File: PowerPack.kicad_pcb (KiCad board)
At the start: 2 copper layers, 79 x 31 mm, 75 parts, among them CN1 XT30PW-M, Q1 WSD3066DN33, U1 IP2368_BZ_VGLIP_C5203723, U2 ME6203A50PG

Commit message: route pcb
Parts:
- C12, C13: value 100nf -> 100nf
- moved U1 0.74 mm to (132.2, 89.2)
- moved R6 0.61 mm to (125.0, 108.1)
- moved CSC1 0.59 mm to (123.7, 89.3)
- moved R2 0.59 mm to (123.7, 90.3)
- moved R8 0.52 mm to (140.5, 108.0)
- moved R23 0.36 mm to (106.8, 106.1)
- moved C11 0.26 mm to (167.9, 106.8)
- moved R25 0.25 mm to (111.8, 106.1)
- moved D1 0.23 mm to (127.3, 95.3)
- moved C3 0.23 mm to (130.9, 95.3)
- moved C13 0.23 mm to (115.5, 101.2)
- moved R22 0.20 mm to (107.5, 101.2)
- moved LED2 0.18 mm to (102.0, 106.8)
- moved R19 0.14 mm to (143.6, 85.9)
- moved R20 0.14 mm to (143.6, 86.9)
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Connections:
- net ISET-MODE renamed Net-(JP1-A)
- JP2 pad 1: BAT-MODE -> Net-(JP2-A)
- R13 pad 1: Net-(U1-BAT_MODE) -> BAT-MODE
- R13 pad 2: BAT-MODE -> Net-(JP2-A)
- U1 pad 46: Net-(U1-BAT_MODE) -> BAT-MODE
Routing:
- net Net-(D3-C): track 0.00 -> 86.8 mm, vias 0 -> 3
- net CIO_CC2: track 0.00 -> 69.4 mm, vias 0 -> 2
- net CIO_CC1: track 0.00 -> 63.5 mm, vias 0 -> 2
- net LED1/SCL: track 0.00 -> 58.5 mm, vias 0 -> 2
- net VBUSR_Source: track 0.00 -> 51.8 mm, vias 1 -> 0
- net LED2/SDA: track 0.00 -> 50.4 mm, vias 0 -> 2
- net Net-(LED1--): track 0.00 -> 50.3 mm, vias 0 -> 2
- net CIO_DN: track 0.00 -> 49.7 mm
- net CIO_DP: track 0.00 -> 47.4 mm, vias 0 -> 2
- net VBUSL_Source: track 0.00 -> 40.0 mm, vias 0 -> 2
- net BAT-MODE: track 0.00 -> 36.9 mm, vias 0 -> 2
- net HLED: track 0.00 -> 31.5 mm, vias 0 -> 2
- net Net-(D3-A): track 0.00 -> 20.3 mm
- net Net-(U1-LG2): track 0.00 -> 20.1 mm
- net Net-(U1-LG1): track 0.00 -> 20.0 mm
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- added copper zone on B.Cu, net GND
- added copper zone on F.Cu, net GND

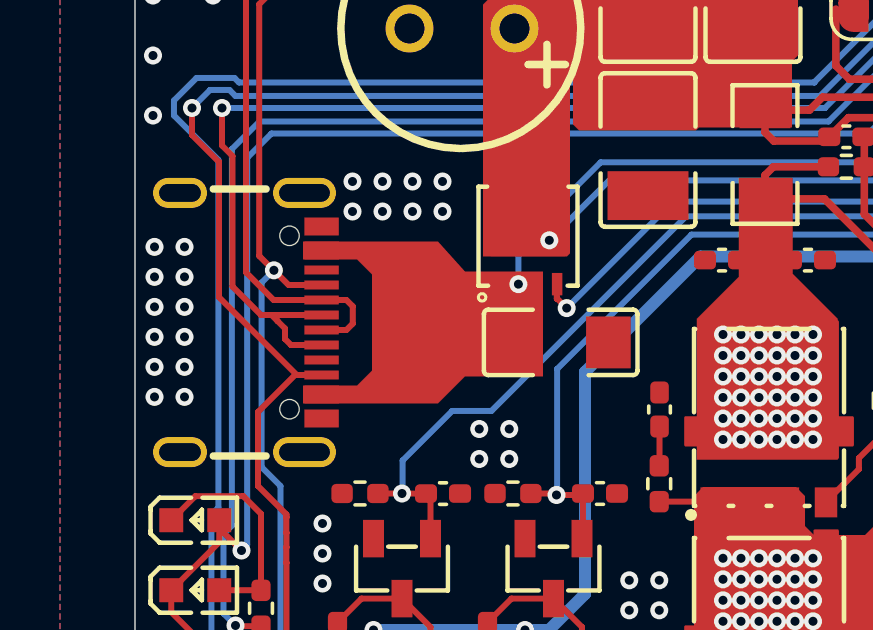
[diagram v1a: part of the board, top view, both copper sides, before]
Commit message: fix usbc connector
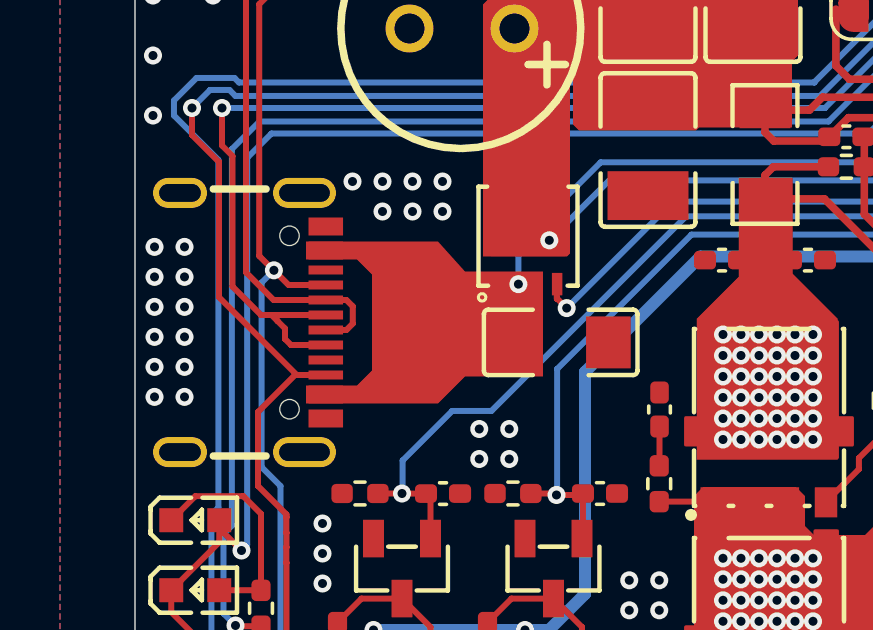
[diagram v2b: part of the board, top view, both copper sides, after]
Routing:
- net GND: vias 240 -> 239
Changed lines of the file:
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@@
 		)
 		(pad "A1B12" smd rect
-			(at -3.2 -2.36 270)
+			(at -3.2 -2.5 270)
 			(size 0.6 1.15)
 			(layers "F.Cu" "F.Mask" "F.Paste")
@@
 		)
 		(pad "A4B9" smd rect
-			(at -2.4 -2.36 270)
+			(at -2.4 -2.5 270)
 			(size 0.6 1.15)
 			(layers "F.Cu" "F.Mask" "F.Paste")
@@
 		)
 		(pad "A5" smd rect
-			(at -1.25 -2.36 270)
+			(at -1.25 -2.5 270)
 			(size 0.3 1.15)
 			(layers "F.Cu" "F.Mask" "F.Paste")
@@
 		)
 		(pad "A6" smd rect
-			(at -0.25 -2.36 270)
+			(at -0.25 -2.5 270)
 			(size 0.3 1.15)
 			(layers "F.Cu" "F.Mask" "F.Paste")
@@
 		)
 		(pad "A7" smd rect
-			(at 0.25 -2.36 270)
+			(at 0.25 -2.5 270)
 			(size 0.3 1.15)
 			(layers "F.Cu" "F.Mask" "F.Paste")
@@
 		)
 		(pad "A8" smd rect
-			(at 1.25 -2.36 270)
+			(at 1.25 -2.5 270)
 			(size 0.3 1.15)
 			(layers "F.Cu" "F.Mask" "F.Paste")
@@
 		)
 		(pad "B1A12" smd rect
-			(at 3.2 -2.36 270)
+			(at 3.2 -2.5 270)
 			(size 0.6 1.15)
 			(layers "F.Cu" "F.Mask" "F.Paste")
@@
 		)
 		(pad "B4A9" smd rect
-			(at 2.4 -2.36 270)
+			(at 2.4 -2.5 270)
 			(size 0.6 1.15)
 			(layers "F.Cu" "F.Mask" "F.Paste")
@@
 		)
 		(pad "B5" smd rect
-			(at 1.75 -2.36 270)
+			(at 1.75 -2.5 270)
 			(size 0.3 1.15)
 			(layers "F.Cu" "F.Mask" "F.Paste")
@@
 		)
 		(pad "B6" smd rect
-			(at 0.75 -2.36 270)
+			(at 0.75 -2.5 270)
 			(size 0.3 1.15)
 			(layers "F.Cu" "F.Mask" "F.Paste")
@@
 		)
 		(pad "B7" smd rect
-			(at -0.75 -2.36 270)
+			(at -0.75 -2.5 270)
 			(size 0.3 1.15)
 			(layers "F.Cu" "F.Mask" "F.Paste")
@@
 		)
 		(pad "B8" smd rect
-			(at -1.75 -2.36 270)
+			(at -1.75 -2.5 270)
 			(size 0.3 1.15)
 			(layers "F.Cu" "F.Mask" "F.Paste")
@@
 	(gr_poly
 		(pts
-			(xy 105.6 92.8) (xy 105.7 92.8) (xy 110.1 92.8) (xy 111 93.8) (xy 113.6 93.8) (xy 113.6 97.3) (xy 111 97.3)
-			(xy 110.1 98.2) (xy 105.6 98.2) (xy 105.6 97.6) (xy 107.4 97.6) (xy 107.9 97.1) (xy 107.9 93.9) (xy 107.4 93.4)
-			(xy 105.6 93.4)
+			(xy 105.7 92.8) (xy 105.7 92.8) (xy 110.1 92.8) (xy 111 93.8) (xy 113.6 93.8) (xy 113.6 97.3) (xy 111 97.3)
+			(xy 110.1 98.2) (xy 105.7 98.2) (xy 105.7 97.6) (xy 107.4 97.6) (xy 107.9 97.1) (xy 107.9 93.9) (xy 107.4 93.4)
+			(xy 105.7 93.4)
 		)
 		(stroke
@@
 	)
 	(segment
-		(start 136.7 90.9)
-		(end 135.62 90.9)
-		(width 0.254)
-		(layer "F.Cu")
-		(net 1)
-	)
-	(segment
 		(start 159.9 102.46)
 		(end 160.9 103.46)
@@
 	)
 	(segment
+		(start 136.7 90.9)
+		(end 135.62 90.9)
+		(width 0.254)
+		(layer "F.Cu")
+		(net 1)
+	)
+	(segment
 		(start 158.4 102.46)
 		(end 159.9 102.46)
@@
 		(size 0.6)
 		(drill 0.3)
-		(layers "F.Cu" "B.Cu")
-		(net 2)
-	)
-	(via
-		(at 107.25 91.8)
-		(size 0.6)
-		(drill 0.3)
